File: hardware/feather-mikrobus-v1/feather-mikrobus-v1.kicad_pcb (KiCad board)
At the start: 2 copper layers, 63.5 x 58.4 mm, 27 parts, among them J1 Adafruit_Feather_socket_heade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, J2 Adafruit_Feather_socket_heade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, J3 mikroBUS_socket_header_left_p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, J4 mikroBUS_socket_header_right_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, SW1 C_and_K_JS102011SAQN, SW2 C_and_K_KMR421GULCLFS, SW3 C_and_K_KMR421GULCLFS

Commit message: [WIP] Update logos
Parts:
- LOGO2: value Flying_Camp_Design_logo_7.35x11mm_silkscreen -> ~; footprint Flying_Camp_Design:Flying_Camp_Design_logo_7.35x11mm_silkscreen -> Flying_Camp_Design:LOGO_FCD_7.4X11MM_SILKSCREEN
- LOGO3: value Adafruit_Feather_logo_13.87x6.33mm_silkscreen -> ~; footprint Flying_Camp_Design:Adafruit_Feather_logo_13.87x6.33mm_silkscreen -> Flying_Camp_Design:LOGO_ADAFRUIT_FEATHER_13.9X6.4_SILKSCREEN
- REF**: value KiCad-Logo_5mm_SilkScreen -> ~; footprint Flying_Camp_Design:KiCad-Logo_5mm_SilkScreen -> Flying_Camp_Design:LOGO_KICAD_13X5MM_SILKSCREEN
- REF**: value OSHW-Logo2_14.6x12mm_SilkScreen -> ~; footprint Flying_Camp_Design:OSHW-Logo2_14.6x12mm_SilkScreen -> Flying_Camp_Design:LOGO_OSHW_14.6X12MM_SILKSCREEN

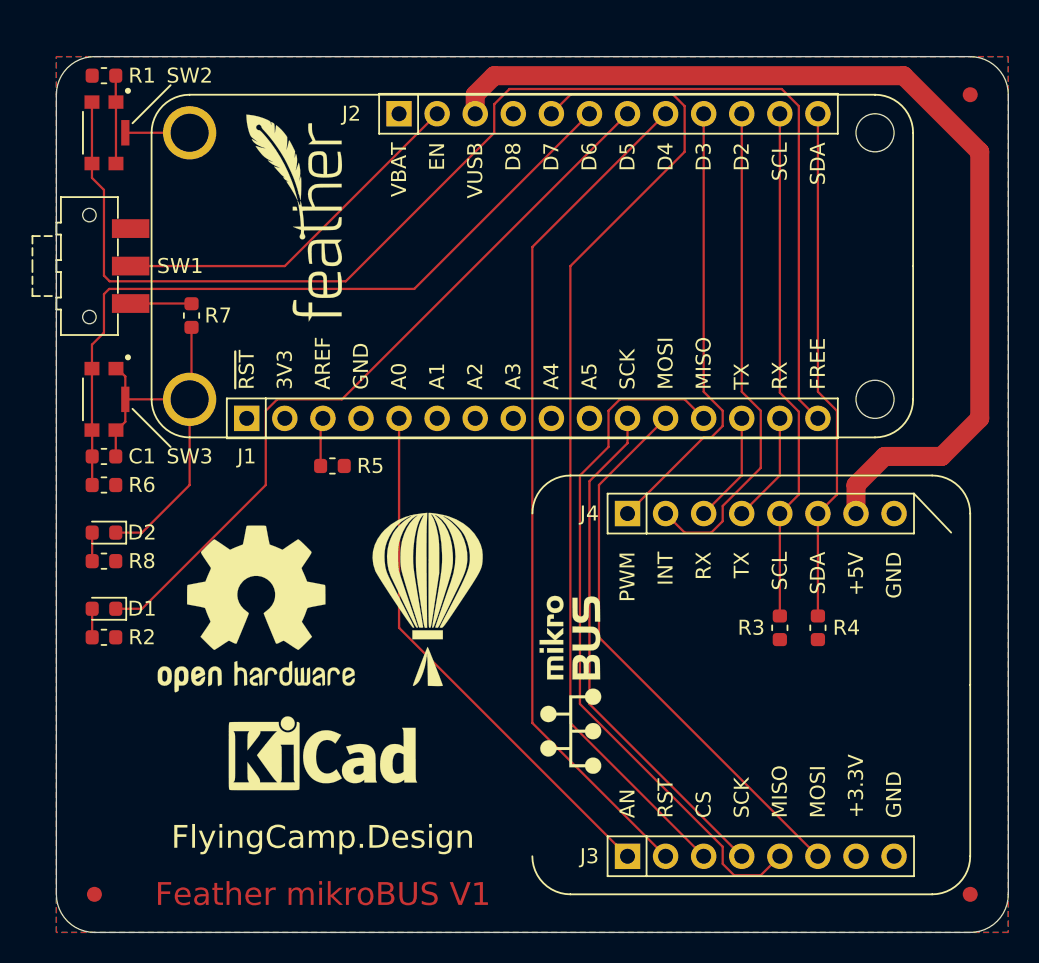
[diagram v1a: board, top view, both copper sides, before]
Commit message: [WIP] Start migration of legacy parts
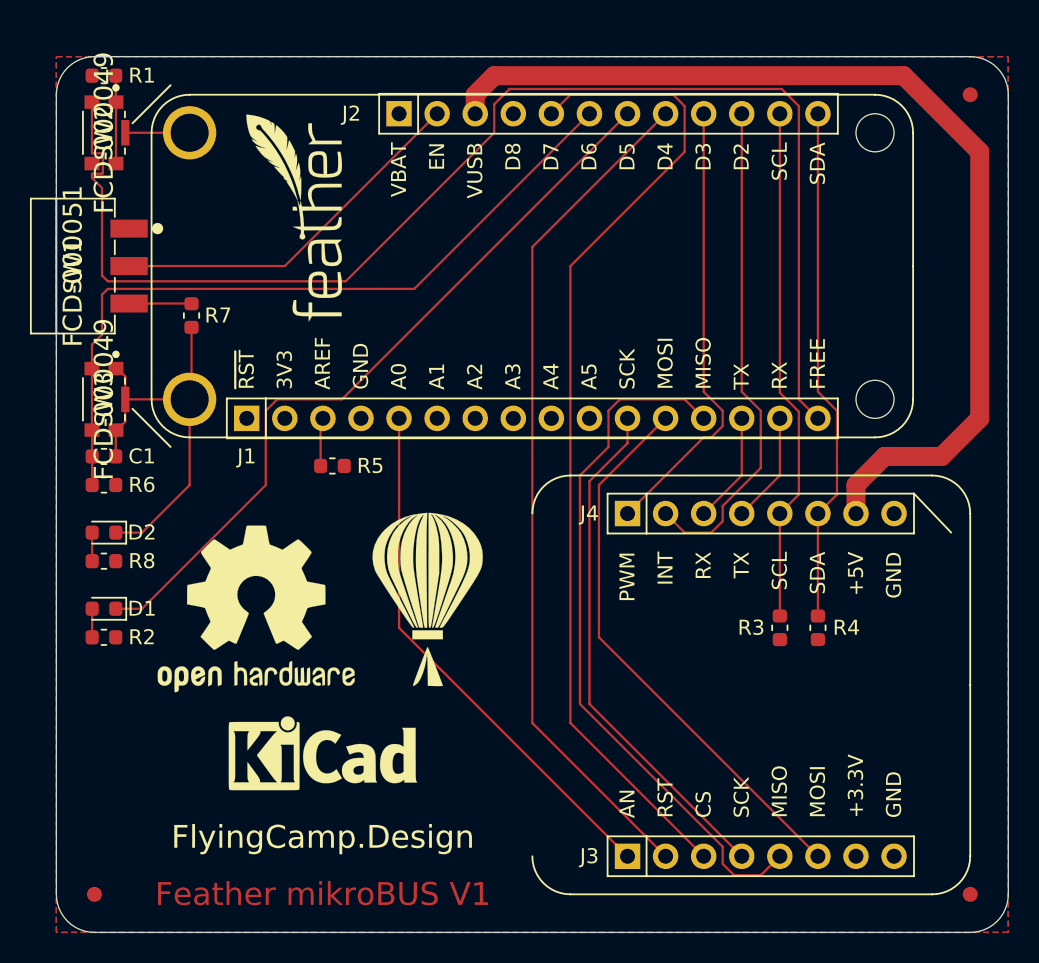
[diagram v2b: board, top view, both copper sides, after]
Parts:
- removed LOGO1: mikroBUS-Logo_11.9x4.1mm_SilkScreen, Flying_Camp_Design:mikroBUS-Logo_11.9x4.1mm_SilkScreen
- C1: value Murata_GRM188R72A104KA35D -> Murata_GRM188R72A104KA35D-Flying_Camp_Design
- D1, D2: value Lite-On_LTST-C193KGKT-5A -> Lite-On_LTST-C193KGKT-5A-Flying_Camp_Design
- FID1, FID2, FID3: value Fiducial_1mm_Mask2mm -> ~; footprint Flying_Camp_Design:Fiducial_1mm_Mask2mm -> Flying_Camp_Design:FIDUCIAL_GLOBAL_1X2MM
- J1: value Adafruit_Feather_socket_header_left_pth -> Adafruit_Feather_socket_header_left_pth-Flying_Camp_Design
- J2: value Adafruit_Feather_socket_header_right_pth -> Adafruit_Feather_socket_header_right_pth-Flying_Camp_Design
- J3: value mikroBUS_socket_header_left_pth -> mikroBUS_socket_header_left_pth-Flying_Camp_Design
- J4: value mikroBUS_socket_header_right_pth -> mikroBUS_socket_header_right_pth-Flying_Camp_Design
- MH1: value Adafruit_Feather_socket_mounting_holes -> Adafruit_Feather_socket_mounting_holes-Flying_Camp_Design
- R1: value Yageo_RC0603JR-071KL -> Yageo_RC0603JR-071KL-Flying_Camp_Design
- R2, R8: value Yageo_RC0603JR-07330RL -> Yageo_RC0603JR-07330RL-Flying_Camp_Design
- R3, R4: value Yageo_RC0603JR-074K7L -> Yageo_RC0603JR-074K7L-Flying_Camp_Design
- R5: value Yageo_RC0603JR-070RL -> Yageo_RC0603JR-070RL-Flying_Camp_Design
- R6: value Yageo_RC0603JR-0710KL -> Yageo_RC0603JR-0710KL-Flying_Camp_Design
- R7: value Yageo_RC0603JR-07100RL -> Yageo_RC0603JR-07100RL-Flying_Camp_Design
- SW1: value C_and_K_JS102011SAQN -> FCD-000051; footprint Flying_Camp_Design:C_and_K_JS102011SAQN -> Flying_Camp_Design:CK_JS102011SAQN
- SW2, SW3: value C_and_K_KMR421GULCLFS -> FCD-000049; footprint Flying_Camp_Design:C_and_K_KMR421GULCLFS -> Flying_Camp_Design:CK_KMR4
- ~: renamed from REF**; footprint Flying_Camp_Design:LOGO_OSHW_14.6X12MM_SILKSCREEN -> Flying_Camp_Design:LOGO_OSHW_14X12MM_SILKSCREEN
- ~: renamed from LOGO2; footprint Flying_Camp_Design:LOGO_FCD_7.4X11MM_SILKSCREEN -> Flying_Camp_Design:LOGO_FCD_8X12MM_SILKSCREEN
- ~: renamed from LOGO3; footprint Flying_Camp_Design:LOGO_ADAFRUIT_FEATHER_13.9X6.4_SILKSCREEN -> Flying_Camp_Design:LOGO_ADAFRUIT_FEATHER_14X7MM_SILKSCREEN
- moved SW1 1.10 mm to (140.8, 100.3)
- renumbered REF** to ~
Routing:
- net /FEATHER_FREE: track 86.7 -> 88.2 mm

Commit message: [WIP] Update Adafruit Feather legacy footprints
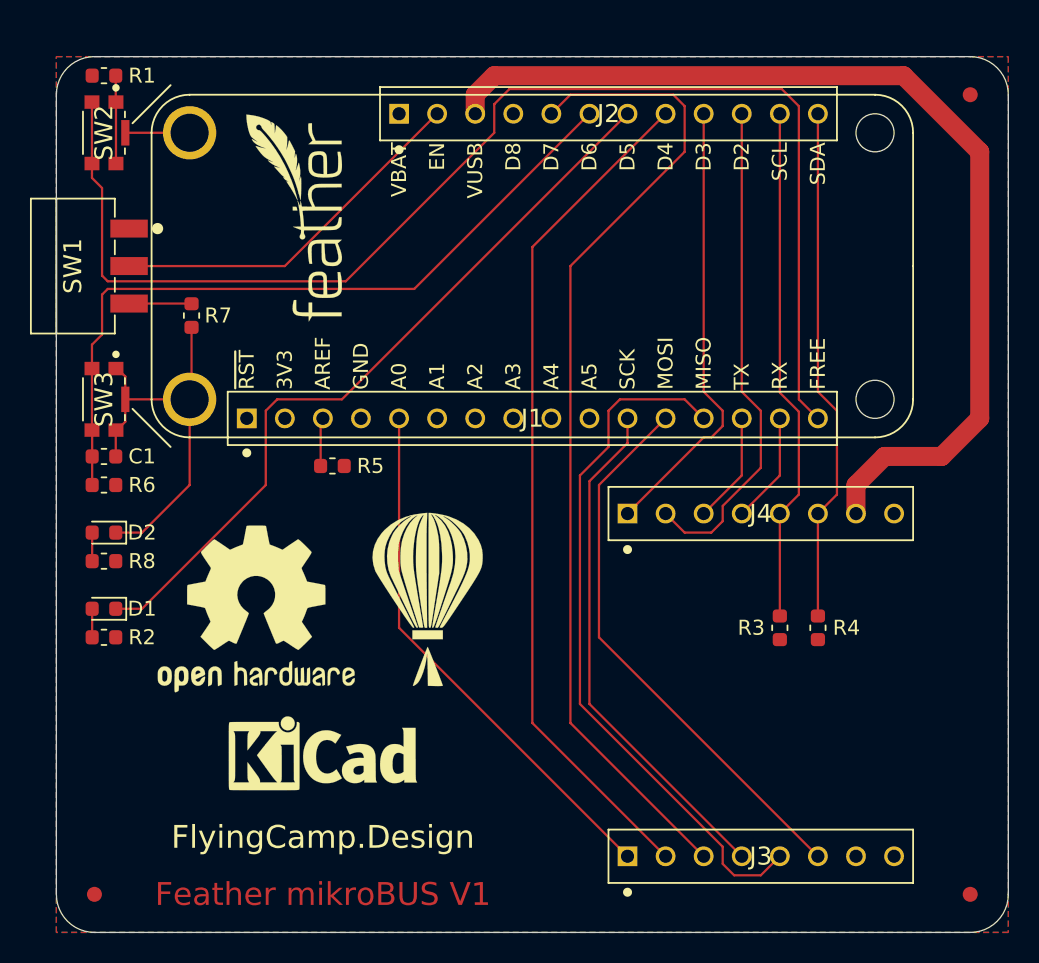
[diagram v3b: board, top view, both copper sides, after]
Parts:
- FID1, FID2, FID3: value ~ -> FIDUCIAL_GLOBAL_1X2MM
- J1: value Adafruit_Feather_socket_header_left_pth-Flying_Camp_Design -> FCD-000047; footprint Flying_Camp_Design:Adafruit_Feather_socket_header_left_pth -> Flying_Camp_Design:TE_6-534237-4
- J2: value Adafruit_Feather_socket_header_right_pth-Flying_Camp_Design -> FCD-000048; footprint Flying_Camp_Design:Adafruit_Feather_socket_header_right_pth -> Flying_Camp_Design:TE_6-534237-0
- J3: value mikroBUS_socket_header_left_pth-Flying_Camp_Design -> FCD-000050; footprint Flying_Camp_Design:mikroBUS_socket_header_left_pth -> Flying_Camp_Design:TE_5-534237-6
- J4: value mikroBUS_socket_header_right_pth-Flying_Camp_Design -> FCD-000050; footprint Flying_Camp_Design:mikroBUS_socket_header_right_pth -> Flying_Camp_Design:TE_5-534237-6
- MOD1: renamed from MH1; value Adafruit_Feather_socket_mounting_holes-Flying_Camp_Design -> MODULE_ADAFRUIT_FEATHER; footprint Flying_Camp_Design:Adafruit_Feather_socket_mounting_holes -> Flying_Camp_Design:MODULE_ADAFRUIT_FEATHER
- moved J1 21.6 mm to (152.4, 110.5), turned to 0 degrees
- moved J4 14.5 mm to (177.8, 116.8), turned to 0 degrees
- moved J3 14.5 mm to (177.8, 139.7), turned to 0 degrees
- moved J2 13.5 mm to (162.6, 90.2), turned to 0 degrees
- turned MOD1 to 90 degrees
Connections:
- SW2 pad 2: /FEATHER_FREE -> /SW2_R
- SW2 pad 4: /SW2_R -> /FEATHER_FREE
- SW3 pad 2: /~USER_SW -> GND
- SW3 pad 4: GND -> /~USER_SW
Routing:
- net /FEATHER_FREE: track 88.2 -> 86.8 mm

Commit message: [WIP] Update legacy mikroBUS symbols
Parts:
- removed the ~ at (155.6, 97.2)
- added MOD2: ~, Flying_Camp_Design:MODULE_MIKROBUS, F.Cu at (186.7, 128.3)
- FID1, FID2, FID3: value FIDUCIAL_GLOBAL_1X2MM -> ~
- MOD1: value MODULE_ADAFRUIT_FEATHER -> ~
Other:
- board text added: "FCD-000053"
- board text removed: "Feather mikroBUS V1"
